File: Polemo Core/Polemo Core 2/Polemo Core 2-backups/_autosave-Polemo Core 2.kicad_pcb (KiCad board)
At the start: 4 copper layers, 40 x 100 mm, 174 parts, among them P1 Header-Male-2.54_2x2, P2 Header-Male-2.54_2x2, Q1 BC847_C2910145, Q2 MMBT5551LT1G, Q3 AO3401A, Q4 AO3401A, Q5 MMBT5551LT1G, U1 ATSAML21G18B-AUT, U10 74LVC1G08GV,125, U11 LT3014BHVES5#TRMPBF, U12 TXU0202DCUR, U13 TLV7031DBVR, U14 TLR341G-GTR, U15 803-87-006-10-001101, U2 XC6209F332MR-G, U3 MC14043BDR2G, U4 LMV793MFX/NOPB, U5 TPS7A2030PDBVR, U6 TLV3201AIDBVT, U7 OPA357AIDBVR, U8 TLR341G-GTR, U9 MF-ASML020/6-2, X1 32.768kHz

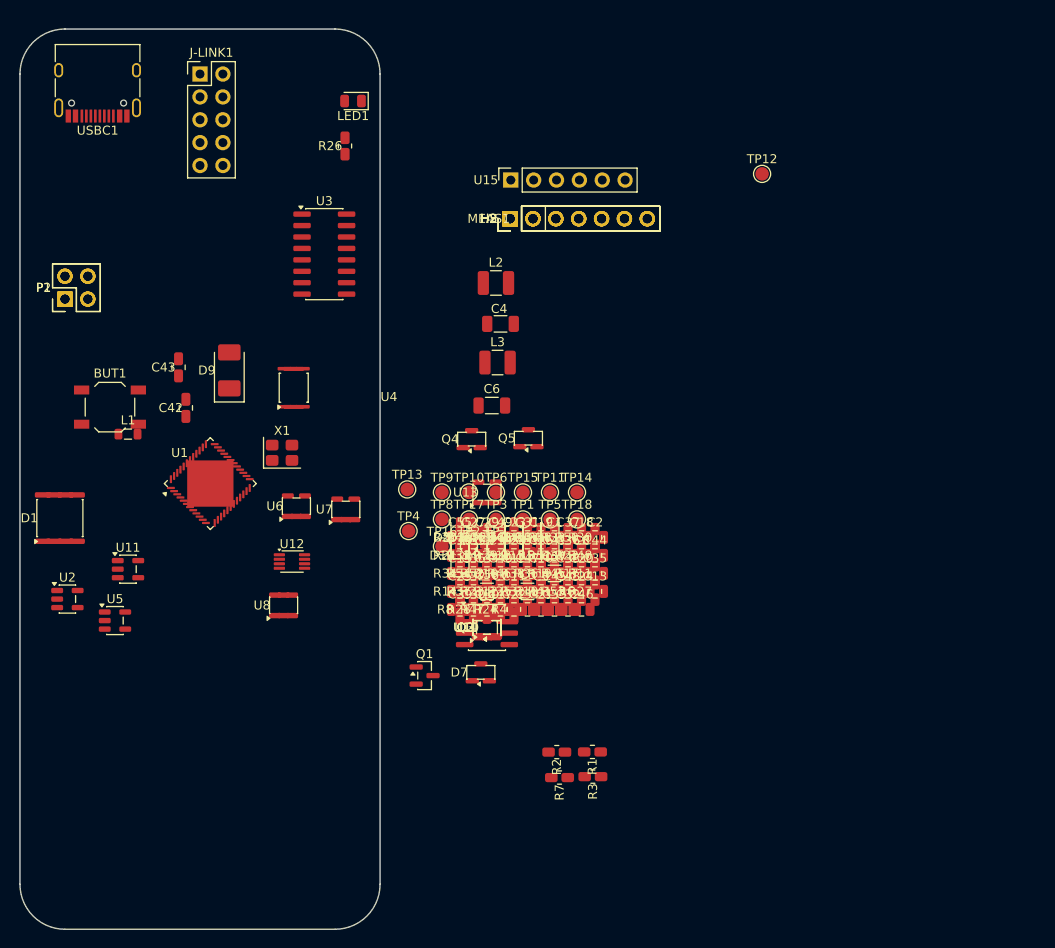
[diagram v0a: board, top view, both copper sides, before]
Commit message: Add scripts for board configuration and component placement on PomeloCore PCB
- Implement `add_board_config.py` to add board outline and upgrade to 4-layer configuration.
- Create `fix_board_config.py` to correctly place board outline at the end of the file and ensure proper layer configuration.
- Develop `place_components.py` to automate component placement based on a reference layout, including defined zones and rotations.
- Introduce `reposition_components.py` to update existing footprint positions on the PCB according to a new layout, ensuring no overlaps.
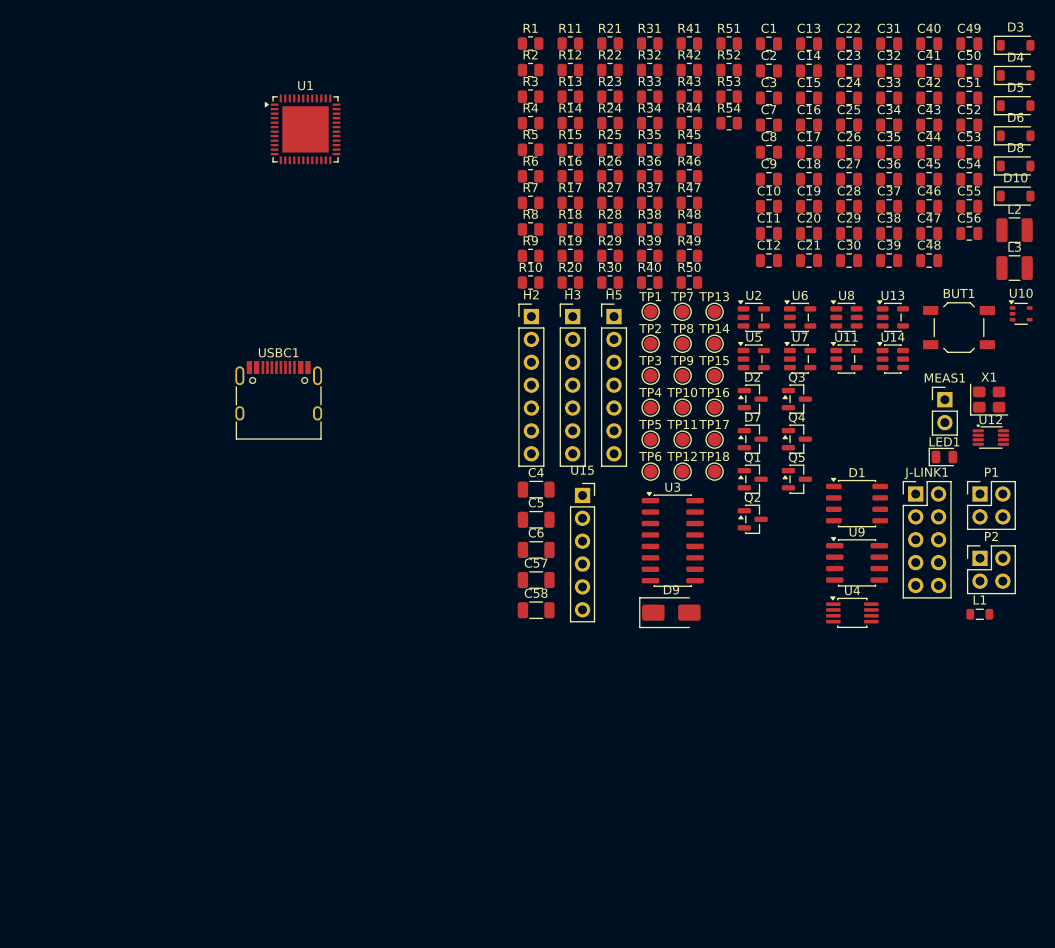
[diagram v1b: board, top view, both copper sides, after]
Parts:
- moved P2 105.6 mm to (156.6, 108.8), turned to 0 degrees
- moved P1 103.9 mm to (156.6, 101.7), turned to 0 degrees
- moved L1 96.7 mm to (156.6, 115.0)
- moved BUT1 94.7 mm to (154.3, 83.2)
- moved J-LINK1 92.2 mm to (149.5, 101.7)
- moved C42 89.5 mm to (151.0, 57.7), turned to 0 degrees
- moved D1 88.6 mm to (143.0, 102.7), turned to 0 degrees
- moved C43 87.6 mm to (151.0, 60.7), turned to 0 degrees
- moved U11 83.2 mm to (141.8, 86.7)
- moved U2 82.4 mm to (131.5, 82.0)
- moved C50 80.3 mm to (155.5, 54.7)
- moved D3 79.5 mm to (160.6, 51.8), turned to 0 degrees
- moved R1 79.0 mm to (106.7, 51.6), turned to 0 degrees
- moved U12 78.8 mm to (157.8, 95.4)
- moved X1 78.8 mm to (157.7, 91.2)
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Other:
- board outline removed
- copper layers 4 -> 2
